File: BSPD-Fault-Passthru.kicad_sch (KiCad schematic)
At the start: 14 parts, among them Q10 SI2318CDS-T1-GE3, Q11 SI2347DS-T1-GE3, Q8 SI2347DS-T1-GE3

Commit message: maintenance push
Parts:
- added R12: 1M, Resistor_SMD:R_0603_1608Metric_Pad0.98x0.95mm_HandSolder, symbol -R-SMD-0603:R-0603-1M-1%-100mW-100PPM
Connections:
- net ERROR-SIG: now also R12.2
- net GND: now also R12.1

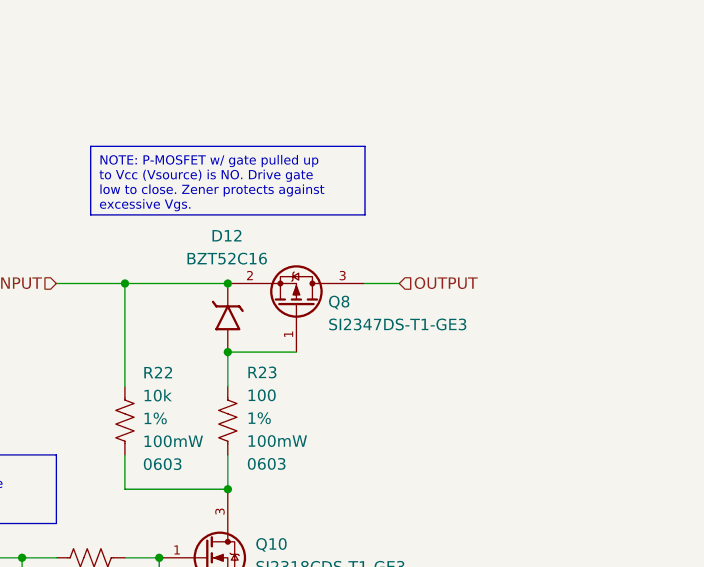
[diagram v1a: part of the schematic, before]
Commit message: updated port directionalities, updated pinout
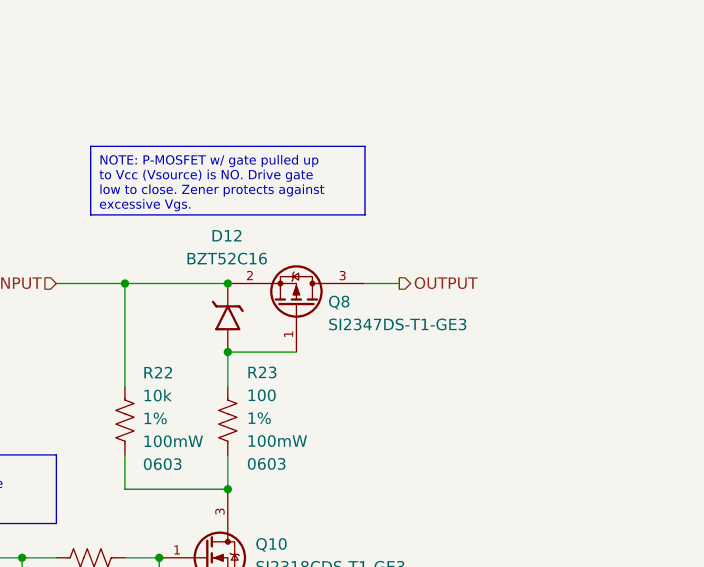
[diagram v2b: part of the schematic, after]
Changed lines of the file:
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@@
 	)
 	(hierarchical_label "OUTPUT"
-		(shape input)
+		(shape output)
 		(at 220.98 110.49 0)
 		(effects

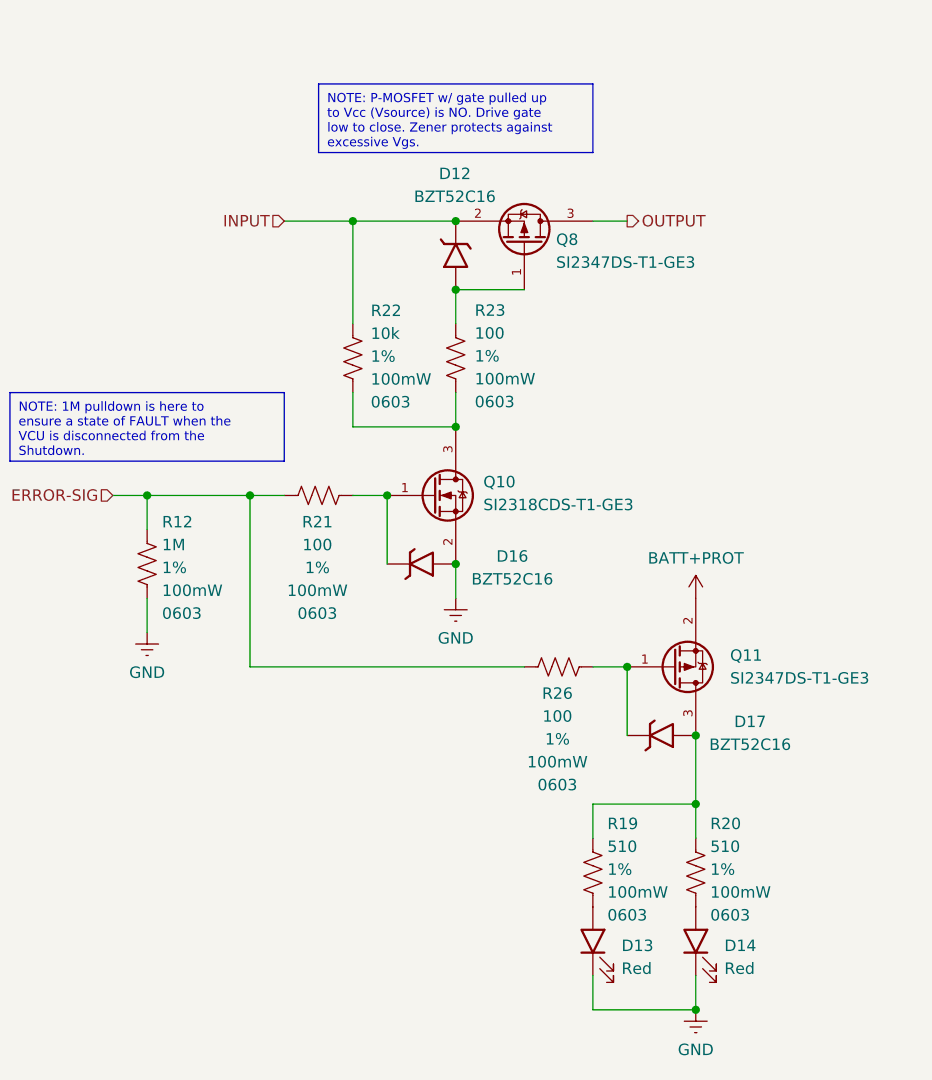
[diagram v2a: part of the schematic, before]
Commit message: Schem is reannotated time to redo all of the layout
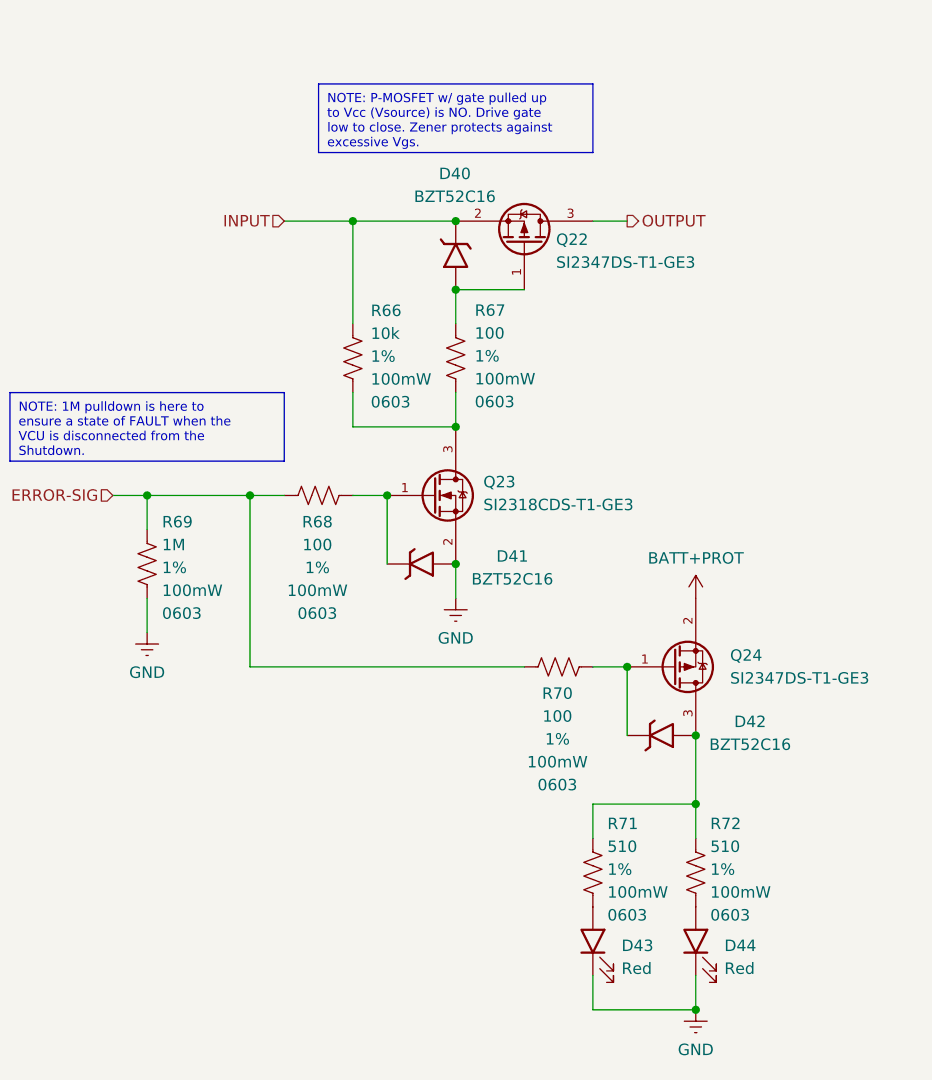
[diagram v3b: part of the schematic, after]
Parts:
- renumbered D12 to D40, D16 to D41, D17 to D42, D13 to D43, D14 to D44, Q8 to Q22, Q10 to Q23, Q11 to Q24, R22 to R66, R23 to R67, R21 to R68, R12 to R69, R26 to R70, R19 to R71, R20 to R72
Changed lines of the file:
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@@
 		(on_board yes)
 		(dnp no)
-		(property "Reference" "D13"
+		(property "Reference" "D43"
 			(at 220.3485 191.0033 90)
 			(effects
@@
 			(project "Shutdown"
 				(path "/624b8e71-6fec-49ba-b7c9-b659e140fc2f/d315361b-ec06-4232-aa8a-9c1cc22253ce"
-					(reference "D13")
+					(reference "D43")
 					(unit 1)
 				)
@@
 		(on_board yes)
 		(dnp no)
-		(property "Reference" "D14"
+		(property "Reference" "D44"
 			(at 231.7785 191.0033 90)
 			(effects
@@
 			(project "Shutdown"
 				(path "/624b8e71-6fec-49ba-b7c9-b659e140fc2f/d315361b-ec06-4232-aa8a-9c1cc22253ce"
-					(reference "D14")
+					(reference "D44")
 					(unit 1)
 				)
@@
 		(on_board yes)
 		(dnp no)
-		(property "Reference" "#PWR026"
+		(property "Reference" "#PWR060"
 			(at 201.93 158.75 0)
 			(effects
@@
 			(project "Shutdown"
 				(path "/624b8e71-6fec-49ba-b7c9-b659e140fc2f/d315361b-ec06-4232-aa8a-9c1cc22253ce"
-					(reference "#PWR026")
+					(reference "#PWR060")
 					(unit 1)
 				)
@@
 		(dnp no)
 		(fields_autoplaced yes)
-		(property "Reference" "Q11"
+		(property "Reference" "Q24"
 			(at 232.41 158.7499 0)
 			(effects
@@
 			(project ""
 				(path "/624b8e71-6fec-49ba-b7c9-b659e140fc2f/d315361b-ec06-4232-aa8a-9c1cc22253ce"
-					(reference "Q11")
+					(reference "Q24")
 					(unit 1)
 				)
@@
 		(on_board yes)
 		(dnp no)
-		(property "Reference" "#PWR011"
+		(property "Reference" "#PWR061"
 			(at 228.6 156.21 0)
 			(effects
@@
 			(project "Shutdown"
 				(path "/624b8e71-6fec-49ba-b7c9-b659e140fc2f/d315361b-ec06-4232-aa8a-9c1cc22253ce"
-					(reference "#PWR011")
+					(reference "#PWR061")
 					(unit 1)
 				)
@@
 		(on_board yes)
 		(dnp no)
-		(property "Reference" "R21"
+		(property "Reference" "R68"
 			(at 186.56 143.931 0)
 			(effects
@@
 			(project "Shutdown"
 				(path "/624b8e71-6fec-49ba-b7c9-b659e140fc2f/d315361b-ec06-4232-aa8a-9c1cc22253ce"
-					(reference "R21")
+					(reference "R68")
 					(unit 1)
 				)
@@
 		(on_board yes)
 		(dnp no)
-		(property "Reference" "D17"
+		(property "Reference" "D42"
 			(at 234.6431 166.1191 0)
 			(effects
@@
 			(project "Shutdown"
 				(path "/624b8e71-6fec-49ba-b7c9-b659e140fc2f/d315361b-ec06-4232-aa8a-9c1cc22253ce"
-					(reference "D17")
+					(reference "D42")
 					(unit 1)
 				)
@@
 		(on_board yes)
 		(dnp no)
-		(property "Reference" "R23"
+		(property "Reference" "R67"
 			(at 204.0399 120.4215 90)
 			(effects
@@
 			(project ""
 				(path "/624b8e71-6fec-49ba-b7c9-b659e140fc2f/d315361b-ec06-4232-aa8a-9c1cc22253ce"
-					(reference "R23")
+					(reference "R67")
 					(unit 1)
 				)
@@
 		(on_board yes)
 		(dnp no)
-		(property "Reference" "Q8"
+		(property "Reference" "Q22"
 			(at 213.0754 112.5486 90)
 			(effects
@@
 			(project "Shutdown"
 				(path "/624b8e71-6fec-49ba-b7c9-b659e140fc2f/d315361b-ec06-4232-aa8a-9c1cc22253ce"
-					(reference "Q8")
+					(reference "Q22")
 					(unit 1)
 				)
@@
 		(on_board yes)
 		(dnp no)
-		(property "Reference" "#PWR012"
+		(property "Reference" "#PWR062"
 			(at 167.64 162.56 0)
 			(effects
@@
 			(project "Shutdown"
 				(path "/624b8e71-6fec-49ba-b7c9-b659e140fc2f/d315361b-ec06-4232-aa8a-9c1cc22253ce"
-					(reference "#PWR012")
+					(reference "#PWR062")
 					(unit 1)
 				)
@@
 		(on_board yes)
 		(dnp no)
-		(property "Reference" "Q10"
+		(property "Reference" "Q23"
 			(at 204.9941 139.4782 0)
 			(effects
@@
 			(project ""
 				(path "/624b8e71-6fec-49ba-b7c9-b659e140fc2f/d315361b-ec06-4232-aa8a-9c1cc22253ce"
-					(reference "Q10")
+					(reference "Q23")
 					(unit 1)
 				)
@@
 		(on_board yes)
 		(dnp no)
-		(property "Reference" "R19"
+		(property "Reference" "R71"
 			(at 218.778 177.4528 90)
 			(effects
@@
 			(project "Shutdown"
 				(path "/624b8e71-6fec-49ba-b7c9-b659e140fc2f/d315361b-ec06-4232-aa8a-9c1cc22253ce"
-					(reference "R19")
+					(reference "R71")
 					(unit 1)
 				)
@@
 		(on_board yes)
 		(dnp no)
-		(property "Reference" "R12"
+		(property "Reference" "R69"
 			(at 169.2922 143.929 90)
 			(effects
@@
 			(project ""
 				(path "/624b8e71-6fec-49ba-b7c9-b659e140fc2f/d315361b-ec06-4232-aa8a-9c1cc22253ce"
-					(reference "R12")
+					(reference "R69")
 					(unit 1)
 				)
@@
 		(on_board yes)
 		(dnp no)
-		(property "Reference" "#PWR027"
+		(property "Reference" "#PWR065"
 			(at 228.6 204.47 0)
 			(effects
@@
 			(project "Shutdown"
 				(path "/624b8e71-6fec-49ba-b7c9-b659e140fc2f/d315361b-ec06-4232-aa8a-9c1cc22253ce"
-					(reference "#PWR027")
+					(reference "#PWR065")
 					(unit 1)
 				)
@@
 		(on_board yes)
 		(dnp no)
-		(property "Reference" "D12"
+		(property "Reference" "D40"
 			(at 201.834 105.2341 90)
 			(effects
@@
 			(project "Shutdown"
 				(path "/624b8e71-6fec-49ba-b7c9-b659e140fc2f/d315361b-ec06-4232-aa8a-9c1cc22253ce"
-					(reference "D12")
+					(reference "D40")
 					(unit 1)
 				)
@@
 		(on_board yes)
 		(dnp no)
-		(property "Reference" "R20"
+		(property "Reference" "R72"
 			(at 230.208 177.4528 90)
 			(effects
@@
 			(project "Shutdown"
 				(path "/624b8e71-6fec-49ba-b7c9-b659e140fc2f/d315361b-ec06-4232-aa8a-9c1cc22253ce"
-					(reference "R20")
+					(reference "R72")
 					(unit 1)
 				)
@@
 		(on_board yes)
 		(dnp no)
-		(property "Reference" "R26"
+		(property "Reference" "R70"
 			(at 213.23 162.981 0)
 			(effects
@@
 			(project "Shutdown"
 				(path "/624b8e71-6fec-49ba-b7c9-b659e140fc2f/d315361b-ec06-4232-aa8a-9c1cc22253ce"
-					(reference "R26")
+					(reference "R70")
 					(unit 1)
 				)
@@
 		(on_board yes)
 		(dnp no)
-		(property "Reference" "R22"
+		(property "Reference" "R66"
 			(at 192.4822 120.4484 90)
 			(effects
@@
 			(project ""
 				(path "/624b8e71-6fec-49ba-b7c9-b659e140fc2f/d315361b-ec06-4232-aa8a-9c1cc22253ce"
-					(reference "R22")
+					(reference "R66")
 					(unit 1)
 				)
@@
 		(on_board yes)
 		(dnp no)
-		(property "Reference" "D16"
+		(property "Reference" "D41"
 			(at 208.2195 147.7433 0)
 			(effects
@@
 			(project "Shutdown"
 				(path "/624b8e71-6fec-49ba-b7c9-b659e140fc2f/d315361b-ec06-4232-aa8a-9c1cc22253ce"
-					(reference "D16")
+					(reference "D41")
 					(unit 1)
 				)

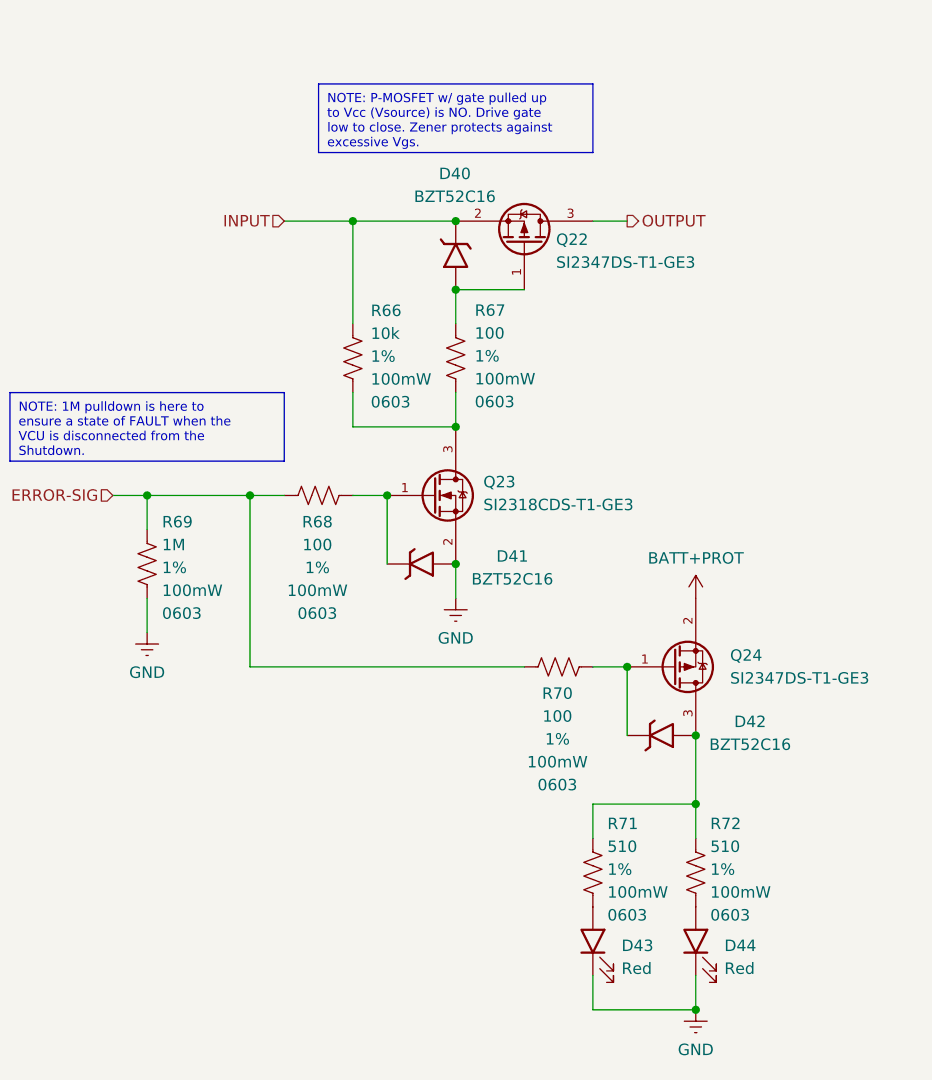
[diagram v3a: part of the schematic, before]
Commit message: Finished shutdown, 0 drc, need to export gerbers
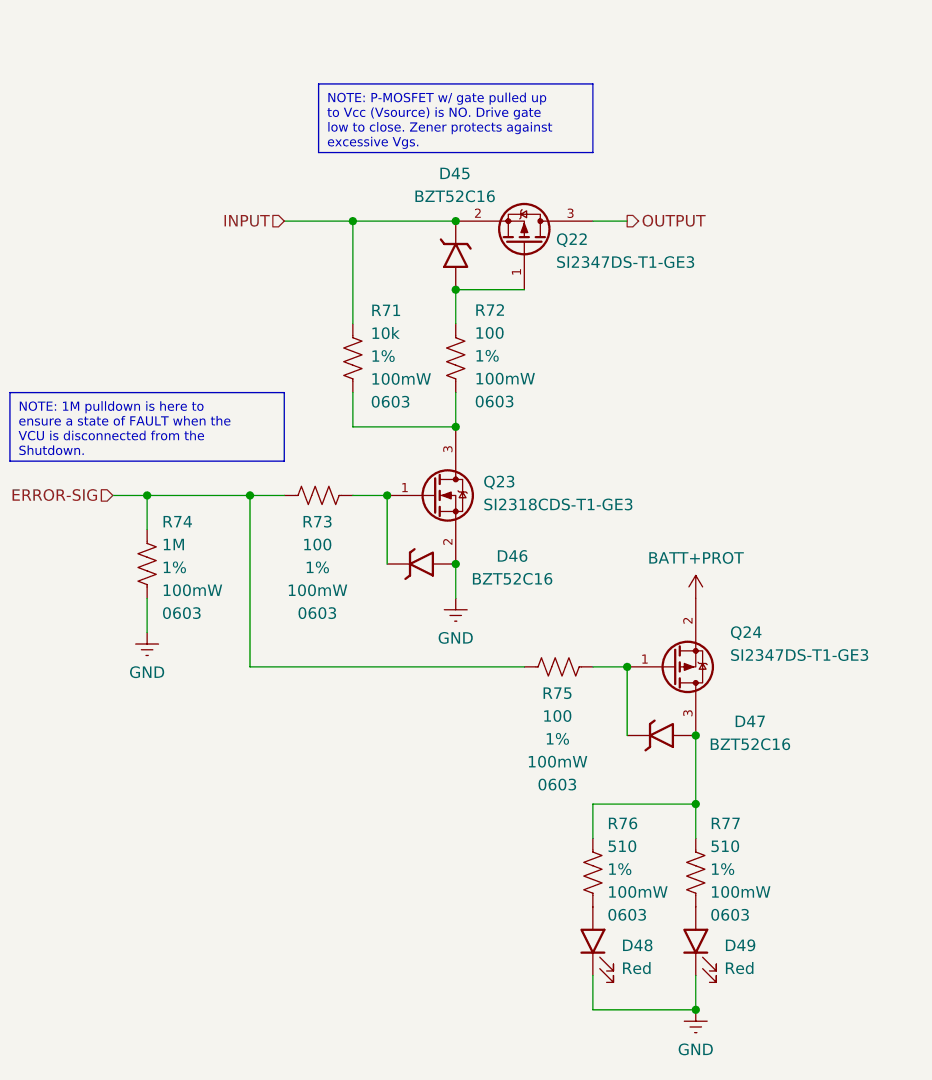
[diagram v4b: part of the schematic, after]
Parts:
- renumbered D40 to D45, D41 to D46, D42 to D47, D43 to D48, D44 to D49, R66 to R71, R67 to R72, R68 to R73, R69 to R74, R70 to R75, R71 to R76, R72 to R77

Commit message: schematic updated to V2 extra crispy
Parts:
- removed D48, D49: Red, LED_SMD:LED_0805_2012Metric, symbol -Diodes-LED:NCD0805R1
- removed R76, R77: 510, Resistor_SMD:R_0603_1608Metric_Pad0.98x0.95mm_HandSolder, symbol -R-SMD-0603:R-0603-510-1%-100mW-100PPM
- added D54, D55: Red, LED_SMD:LED_0805_2012Metric, symbol -Diodes-LED:NCD0805R1
- added R74: 1M, Resistor_SMD:R_0603_1608Metric_Pad0.98x0.95mm_HandSolder, symbol -R-SMD-0603:R-0603-1M-1%-100mW-100PPM
- added R80, R81: 680, Resistor_SMD:R_0603_1608Metric_Pad0.98x0.95mm_HandSolder, symbol -R-SMD-0603:R-0603-680-1%-100mW-100PPM
- renumbered D45 to D51, D46 to D52, D47 to D53, Q22 to Q23, Q23 to Q24, Q24 to Q25, R71 to R75, R72 to R76, R73 to R77, R74 to R78, R75 to R79
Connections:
- net GND: now also D54.1 (K), D55.1 (K), R74.1
- net OUTPUT: now also R74.2
- net at D53.2 (A), Q25.3 (D): now also R80.2, R81.2
- new net: D55.2 (A), R81.1
- new net: D54.2 (A), R80.1
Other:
- moved on the sheet: D51, D52, D53, Q23, Q24, Q25, R75, R76, R77, R78, R79
